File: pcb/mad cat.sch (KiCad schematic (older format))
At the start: 271 parts, among them J1 Conn_01x04, J2 Conn_02x03_Odd_Even, SW0,0 ESC, SW0,1 ESC/F1, SW0,10 F9, SW0,10-1 F10, SW0,11 F10, SW0,11-1 F11, SW0,12 F11, SW0,12-1 F12, SW0,13 F12/PRT, SW0,14 INS, SW0,15 HOME, SW0,16 PGUP, SW0,2 F1, SW0,2-1 F2, SW0,3 F2, SW0,3-1 F3, SW0,4 F3, SW0,4-1 F4, SW0,5 F4, SW0,5-1 F5, SW0,6 F5, SW0,6-1 F6, SW0,7 F6, SW0,7-1 F7, SW0,8 F7, SW0,8-1 F8, SW0,9 F8, SW0,9-1 F9, SW1,0 PF1, SW1,0-1 PF1, SW1,1 TILDE, SW1,10 9, SW1,11 0, SW1,12 -, SW1,13 =, SW1,14 BACKSPACE, SW1,14-1 S_BS_L, SW1,15 END, SW1,16 PGDN, SW1,2 1, SW1,3 2, SW1,4 3, SW1,5 4, SW1,6 5, SW1,7 6, SW1,8 7, SW1,9 8, SW2,0 PF2, SW2,0-1 PF2, SW2,1 TAB, SW2,10 O, SW2,11 P, SW2,12 [, SW2,13 ], SW2,14 \\, SW2,15 S_BS_R, SW2,16 PRT, SW2,2 Q, SW2,3 W, SW2,4 E, SW2,5 R, SW2,6 T, SW2,7 Y, SW2,8 U, SW2,9 I, SW3,0 PF3, SW3,0-1 PF3, SW3,1 CAPS, SW3,1-1 ST_CAPS, SW3,10 L, SW3,11 COLONS, SW3,12 QUOTE, SW3,13 ISO_#, SW3,14 ENT, SW3,14-1 ISO_ENT, SW3,15 DEL, SW3,15-1 DEL, SW3,15-2 DEL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

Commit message: back to editing pcb
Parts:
- added SW1,15-1: HOME, MX_SMK_2:MX_100, symbol keyboard_parts:SW_PUSH
- added SW1,16-1: PGUP, MX_SMK_2:MX_100, symbol keyboard_parts:SW_PUSH
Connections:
- net c15: now also SW1,15-1.2
- net c16: now also SW1,16-1.2
- net at D33.2, SW1,15.1: now also SW1,15-1.1
- net at D34.2, SW1,16.1: now also SW1,16-1.1
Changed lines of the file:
@@
 Connection ~ 12600 2050
 Wire Wire Line
-	12600 2050 12600 1550
+	12600 2050 12600 1950
 Connection ~ 12600 2550
 Wire Wire Line
@@
 Connection ~ 13350 2050
 Wire Wire Line
-	13350 2050 13350 1550
+	13350 2050 13350 1950
 Connection ~ 13350 2550
 Connection ~ 13350 3050
@@
 Wire Wire Line
 	9000 4250 9750 4250
+$Comp
+L keyboard_parts:SW_PUSH SW1,16-1
+U 1 1 5D092AB2
+P 13050 1950
+F 0 "SW1,16-1" H 13050 2100 50  0000 C CNN
+F 1 "PGUP" H 13050 1850 50  0000 C CNN
+F 2 "MX_SMK_2:MX_100" H 13050 1950 60  0001 C CNN
+F 3 "" H 13050 1950 60  0000 C CNN
+	1    13050 1950
+	1    0    0    -1
+$EndComp
+Connection ~ 13350 1950
+Wire Wire Line
+	13350 1950 13350 1550
+Wire Wire Line
+	12750 1950 12750 2050
+Connection ~ 12750 2050
+$Comp
+L keyboard_parts:SW_PUSH SW1,15-1
+U 1 1 5D0B2107
+P 12300 1950
+F 0 "SW1,15-1" H 12300 2100 50  0000 C CNN
+F 1 "HOME" H 12300 1850 50  0000 C CNN
+F 2 "MX_SMK_2:MX_100" H 12300 1950 60  0001 C CNN
+F 3 "" H 12300 1950 60  0000 C CNN
+	1    12300 1950
+	1    0    0    -1
+$EndComp
+Connection ~ 12600 1950
+Wire Wire Line
+	12600 1950 12600 1550
+Wire Wire Line
+	12000 1950 12000 2050
+Connection ~ 12000 2050
 $EndSCHEMATC

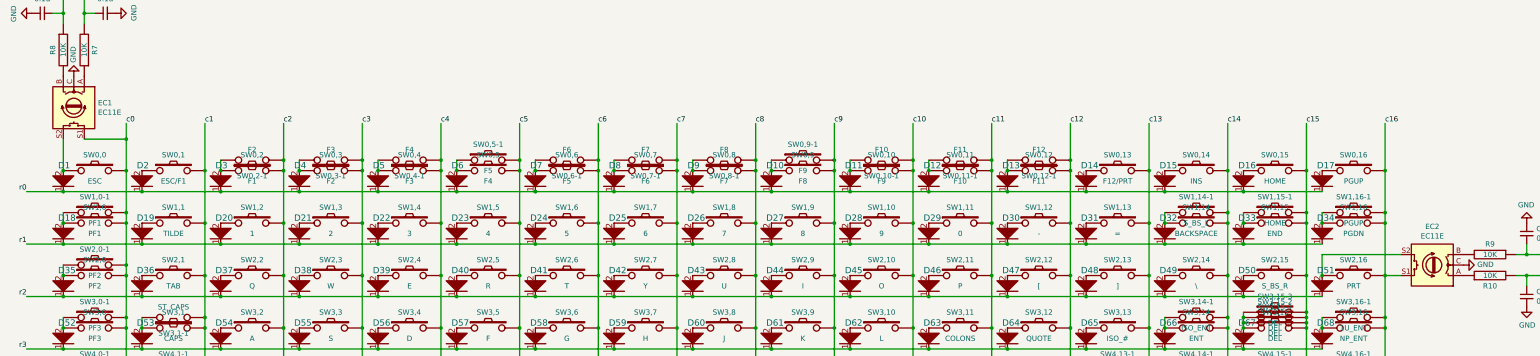
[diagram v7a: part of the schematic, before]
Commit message: added panel mount footprints
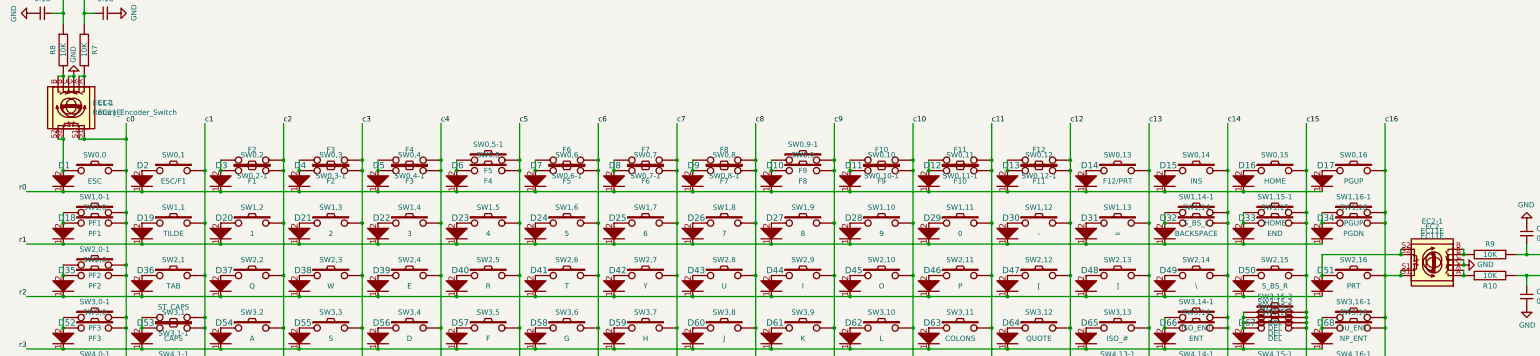
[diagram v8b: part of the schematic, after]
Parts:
- added EC1-1: Rotary_Encoder_Switch, keebs:ec11b, symbol Device:Rotary_Encoder_Switch
- added EC2-1: EC11E, keebs:ec11b, symbol Device:Rotary_Encoder_Switch
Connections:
- net GND: now also EC1-1.C, EC2-1.C
- net c0: now also EC1-1.S1
- net c16: now also EC2-1.S1
- net at EC2.A, R10.1: now also EC2-1.A
- net at EC2.B, R9.2: now also EC2-1.B
- net at D51.2, EC2.S2, SW2,16.1: now also EC2-1.S2
- net at EC1.A, R7.1: now also EC1-1.A
- net at EC1.B, R8.2: now also EC1-1.B
- net at D1.2, EC1.S2, SW0,0.1: now also EC1-1.S2
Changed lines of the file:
@@
 	12000 1950 12000 2050
 Connection ~ 12000 2050
+$Comp
+L Device:Rotary_Encoder_Switch EC1-1
+U 1 1 5D1251FB
+P 800 950
+F 0 "EC1-1" V 754 1180 50  0000 L CNN
+F 1 "Rotary_Encoder_Switch" V 845 1180 50  0000 L CNN
+F 2 "keebs:ec11b" H 650 1110 50  0001 C CNN
+F 3 "~" H 800 1210 50  0001 C CNN
+	1    800  950
+	0    1    1    0
+$EndComp
+Wire Wire Line
+	900  1250 950  1250
+Connection ~ 950  1250
+Wire Wire Line
+	700  1250 750  1250
+Connection ~ 750  1250
+Wire Wire Line
+	700  650  750  650
+Connection ~ 750  650
+Wire Wire Line
+	800  650  850  650
+Connection ~ 850  650
+Wire Wire Line
+	900  650  950  650
+Connection ~ 950  650
+$Comp
+L Device:Rotary_Encoder_Switch EC2-1
+U 1 1 5D1CB5B1
+P 13800 2400
+F 0 "EC2-1" H 13800 2033 50  0000 C CNN
+F 1 "EC11E" H 13800 2124 50  0000 C CNN
+F 2 "keebs:ec11b" H 13650 2560 50  0001 C CNN
+F 3 "~" H 13800 2660 50  0001 C CNN
+	1    13800 2400
+	-1   0    0    1
+$EndComp
+Wire Wire Line
+	13500 2500 13500 2550
+Connection ~ 13500 2550
+Wire Wire Line
+	13500 2300 13500 2350
+Connection ~ 13500 2350
+Wire Wire Line
+	14100 2300 14100 2350
+Connection ~ 14100 2350
+Wire Wire Line
+	14100 2400 14100 2450
+Connection ~ 14100 2450
+Wire Wire Line
+	14100 2500 14100 2550
+Connection ~ 14100 2550
 $EndSCHEMATC
